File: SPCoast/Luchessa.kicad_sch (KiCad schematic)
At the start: 79 parts, among them SW7783 783, SW7795 795, SW7799 799, SW7900 795

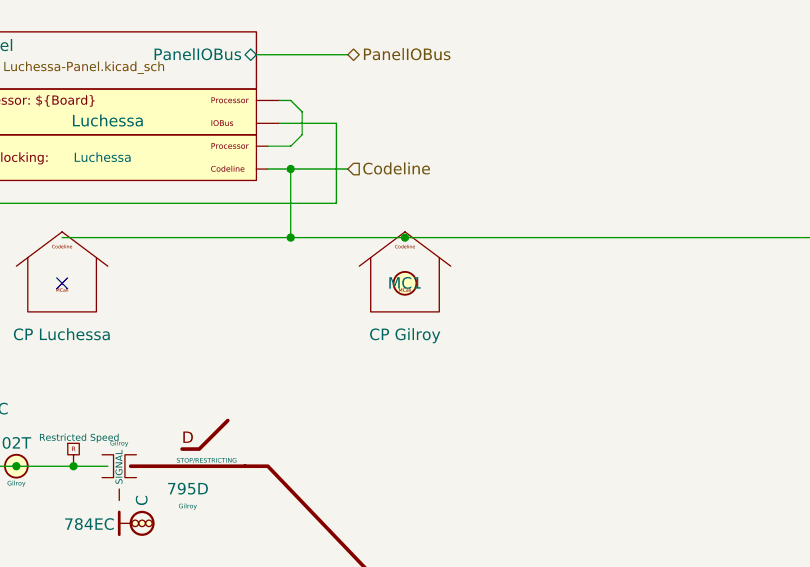
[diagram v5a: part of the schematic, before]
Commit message: feat(spcoast): per-pin token fields on the panels, lamp Indication expressions, maintainer calls named 1MC
Applies the symbol rulings of 2026-10-28 to every sheet: the lib_symbols
caches of the changed symbols are the library's copies (this also clears
the stale PanelMCall and MaintainerCall caches), and every placed
instance gets the new hidden Control.*/Indication.* fields, loses
PanelLock Invert, and PanelMCall's whole-symbol Control and Indication
(Pin.MCK binary). Model lamps' IndicationToken becomes Indication: each
comma-separated circuit gets its K, qualifiers kept, joined with " | "
(795T1,01T,799T1 -> 795T1K | 01TK | 799T1K).

Maintainer calls in Christopher (1, 2), Corporal, Luchessa and Sargent
follow Gilroy Interchange (5dad54f): Value MC<n> -> <n>, Name ${Value}MC,
and the separate PanelMCall-Lamp is replaced by unit 2 of the same
PanelMCall at the old lamp's position, so its MCK pin sits where the
LAMP pin was. The old lamps' Column pin touched PanelColumn pin 8
directly (no wire); that pin is now unconnected, as on Gilroy
Interchange. Gilroy Interchange's local MaintainerCall_1 cache and its
two trackplan calls lose Indication.

Verified: fresh netlist before/after: components 752 -> 747 (the five
lamps), nets 1028 -> 1028; each old LAMP-pin net now holds the lever's
unit-2 MCK pin (pin 3) on the same expander pin (B1, pin 9); the levers'
nets are renamed only (~{S} -> ~{MCS}, unit suffix A); no other net
changed. Every field difference is an intended one. ERC 18 -> 1
violations (lib_symbol_mismatch 17 -> 0; pre-existing Sargent AUX1
pin_not_connected remains).

Co-Authored-By: Claude Opus 5.5 <noreply@anthropic.com>
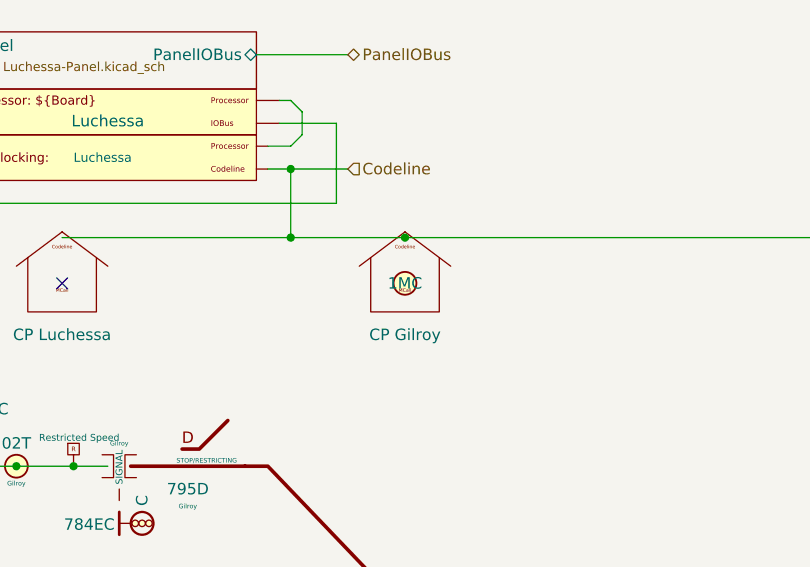
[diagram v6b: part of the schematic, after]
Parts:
- MC7001: value MC1 -> 1; Name ${Value} -> ${Value}MC
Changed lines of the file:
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@@
 			)
 		)
-		(property "Value" "MC1"
+		(property "Value" "1"
 			(at 109.22 49.53 0)
+			(hide yes)
 			(show_name no)
 			(do_not_autoplace no)
@@
 			)
 		)
-		(property "Name" "${Value}"
+		(property "Name" "${Value}MC"
 			(at 109.22 49.53 0)
-			(hide yes)
 			(show_name no)
 			(do_not_autoplace no)

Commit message: feat(symbols,spcoast): track circuits state their Indication; virtual circuits list Members
The owner's edit, 2026-10-29. Every Track Circuit symbol (plain, RED,
Yellow, Virtual) carries Indication=${Name}K: the token a local circuit
reports and a remote consumer (Sargent's Corporal:2NAT) consumes, so
both sides state it and match token to token. Track Circuit_Virtual's
IndicationToken becomes Members (the local circuits it is made of, not
tokens), with Display=${Value}: [${Members}]. Sargent's HBA gets a
no-connect on its unused pin. The panel sheets are re-saved by KiCad
with no field changes.

Verified:
- netlist field diff against 69e87ec: 747 components, none added or
  removed; the only changes are Indication added on 63 track circuits
  (26 Track Circuit, 35 Yellow, 2 Virtual) and IndicationToken renamed
  to Members on TC15032 and TC15034
- ERC: 0 violations (was 1, Sargent AUX1 pin_not_connected)
- Subdivision lint_symbol_fields: 100 symbols, 0 errors, 0 warnings
- Subdivision fresh compile: 0 errors, 0 warnings, 8 info, 2 missing;
  consumer.legacy_token no longer fires

Co-Authored-By: Claude Opus 5.5 <noreply@anthropic.com>
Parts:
- TC7001, TC7002, TC7003, TC7004, TC7005, TC7006: Indication (none) -> ${Name}K
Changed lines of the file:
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@@
 		)
 		(property "Value" "2NAT"
-			(at 214.63 83.82 0)
+			(at 214.63 88.9 0)
+			(hide yes)
 			(show_name no)
-			(do_not_autoplace no)
+			(do_not_autoplace yes)
 			(effects
 				(font
@@
 			)
 		)
+		(property "Indication" "${Name}K"
+			(at 215.9 92.71 0)
+			(hide yes)
+			(show_name no)
+			(do_not_autoplace no)
+			(effects
+				(font
+					(size 1.27 1.27)
+				)
+			)
+		)
 		(pin "1"
 		)
@@
 		)
 		(property "Value" "1NAT"
-			(at 214.63 100.33 0)
+			(at 214.63 105.41 0)
+			(hide yes)
 			(show_name no)
-			(do_not_autoplace no)
+			(do_not_autoplace yes)
 			(effects
 				(font
@@
 			)
 		)
+		(property "Indication" "${Name}K"
+			(at 215.9 109.22 0)
+			(hide yes)
+			(show_name no)
+			(do_not_autoplace no)
+			(effects
+				(font
+					(size 1.27 1.27)
+				)
+			)
+		)
 		(pin "1"
 		)
@@
 		)
 		(property "Value" "02T"
-			(at 66.04 67.31 0)
+			(at 66.04 72.39 0)
+			(hide yes)
 			(show_name no)
-			(do_not_autoplace no)
+			(do_not_autoplace yes)
 			(effects
 				(font
@@
 			)
 		)
+		(property "Indication" "${Name}K"
+			(at 67.31 76.2 0)
+			(hide yes)
+			(show_name no)
+			(do_not_autoplace no)
+			(effects
+				(font
+					(size 1.27 1.27)
+				)
+			)
+		)
 		(pin "1"
 		)
@@
 		)
 		(property "Value" "01T"
-			(at 137.16 83.82 0)
+			(at 137.16 88.9 0)
+			(hide yes)
 			(show_name no)
-			(do_not_autoplace no)
+			(do_not_autoplace yes)
 			(effects
 				(font
@@
 			)
 		)
+		(property "Indication" "${Name}K"
+			(at 138.43 92.71 0)
+			(hide yes)
+			(show_name no)
+			(do_not_autoplace no)
+			(effects
+				(font
+					(size 1.27 1.27)
+				)
+			)
+		)
 		(pin "1"
 		)
@@
 		)
 		(property "Value" "3NAT"
-			(at 214.63 67.31 0)
+			(at 214.63 72.39 0)
+			(hide yes)
 			(show_name no)
-			(do_not_autoplace no)
+			(do_not_autoplace yes)
 			(effects
 				(font
@@
 			)
 		)
+		(property "Indication" "${Name}K"
+			(at 215.9 76.2 0)
+			(hide yes)
+			(show_name no)
+			(do_not_autoplace no)
+			(effects
+				(font
+					(size 1.27 1.27)
+				)
+			)
+		)
 		(pin "1"
 		)
@@
 		)
 		(property "Value" "1SAT"
-			(at 50.8 83.82 0)
+			(at 50.8 88.9 0)
+			(hide yes)
 			(show_name no)
-			(do_not_autoplace no)
+			(do_not_autoplace yes)
 			(effects
 				(font
@@
 			(hide yes)
 			(show_name no)
+			(do_not_autoplace no)
+			(effects
+				(font
+					(size 1.27 1.27)
+				)
+			)
+		)
+		(property "Indication" "${Name}K"
+			(at 52.07 92.71 0)
+			(hide yes)
+			(show_name no)

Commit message: feat(symbols): switches and field lamps state their indication token
A switch states its OS circuit's token, Indication=${TC}K, on Switch_Dual,
Switch_Lock, Switch_Powered, Switch_Powered_Diag, Switch_Powered_Small and
Derail_TC; symbols with no TC (Derail, Switch_Manual, Switch_Manual_Sensed,
Switch_Powered_NO_TC) carry the field present and empty. The AUXILIARY field
lamp states Indication=${Name}K. The four NFLK/SFLK lamps in Luchessa and
Watsonville are renamed NFL/SFL, so their tokens stay NFLK/SFLK. The
sheets are updated from the library.

Verified:
- fresh kicad-cli netlist vs HEAD 6ce30b3: 747 components each, 46 field
  changes: 31 switch/derail Indication, HBA Indication=HBAK, the four
  NFL/SFL renames with their Indication, and MC5001's library entry name
  (MaintainerCall_1 -> MaintainerCall); nothing else
- kicad-cli ERC: 0 violations
- tools/contract/lint_symbol_fields.py: 100 symbols, 0 errors, 0 warnings
- compile_layout.py: 0 errors, 0 warnings, 8 info, 2 missing (unchanged)

Co-Authored-By: Claude Opus 5.5 <noreply@anthropic.com>
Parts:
- FLK7001: value NFLK -> NFL; Indication (none) -> ${Name}K
- FLK7002: value SFLK -> SFL; Indication (none) -> ${Name}K
- SW7783, SW7795, SW7799: Indication (none) -> ${TC}K
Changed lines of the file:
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@@
 			)
 		)
-		(property "Value" "SFLK"
+		(property "Value" "SFL"
 			(at 220.98 40.64 0)
 			(show_name no)
@@
 			)
 		)
+		(property "Indication" "${Name}K"
+			(at 220.98 43.18 0)
+			(hide yes)
+			(show_name no)
+			(do_not_autoplace no)
+			(effects
+				(font
+					(size 1.27 1.27)
+				)
+			)
+		)
 		(pin "1"
 		)
@@
 			)
 		)
+		(property "Indication" "${TC}K"
+			(at 172.72 86.36 0)
+			(hide yes)
+			(show_name no)
+			(do_not_autoplace no)
+			(effects
+				(font
+					(size 1.27 1.27)
+				)
+			)
+		)
 		(pin "2"
 		)
@@
 			)
 		)
+		(property "Indication" "${TC}K"
+			(at 109.22 86.36 0)
+			(hide yes)
+			(show_name no)
+			(do_not_autoplace no)
+			(effects
+				(font
+					(size 1.27 1.27)
+				)
+			)
+		)
 		(pin "3"
 		)
@@
 			)
 		)
-		(property "Value" "NFLK"
+		(property "Value" "NFL"
 			(at 214.63 40.64 0)
 			(show_name no)
@@
 			)
 		)
+		(property "Indication" "${Name}K"
+			(at 214.63 43.18 0)
+			(hide yes)
+			(show_name no)
+			(do_not_autoplace no)
+			(effects
+				(font
+					(size 1.27 1.27)
+				)
+			)
+		)
 		(pin "1"
 		)
@@
 			)
 		)
+		(property "Indication" "${TC}K"
+			(at 71.12 86.36 0)
+			(hide yes)
+			(show_name no)
+			(do_not_autoplace no)
+			(effects
+				(font
+					(size 1.27 1.27)
+				)
+			)
+		)
 		(pin "2"
 		)
@@
 			(at 85.09 69.85 0)
 			(hide yes)
+			(show_name no)
+			(do_not_autoplace no)
+			(effects
+				(font
+					(size 1.27 1.27)
+				)
+			)
+		)
+		(property "Indication" ""
+			(at 85.09 69.85 0)
+			(hide yes)
